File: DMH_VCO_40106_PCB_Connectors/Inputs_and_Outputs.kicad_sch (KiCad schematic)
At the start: 18 parts, among them J1 TS_Jack_6.35mm_Sw, J150 Conn_01x12, J2 TS_Jack_6.35mm_Sw, J200 IDC_02x05, J3 TS_Jack_6.35mm_Sw, J4 TS_Jack_6.35mm_Sw, J5 TS_Jack_6.35mm_Sw, J6 TS_Jack_6.35mm_Sw, J7 TS_Jack_6.35mm_Sw, J8 TS_Jack_6.35mm_Sw, J9 TS_Jack_6.35mm_Sw, SW1 SW_SPDT_321_OnOff, SW2 SW_SPDT_321_OnOff

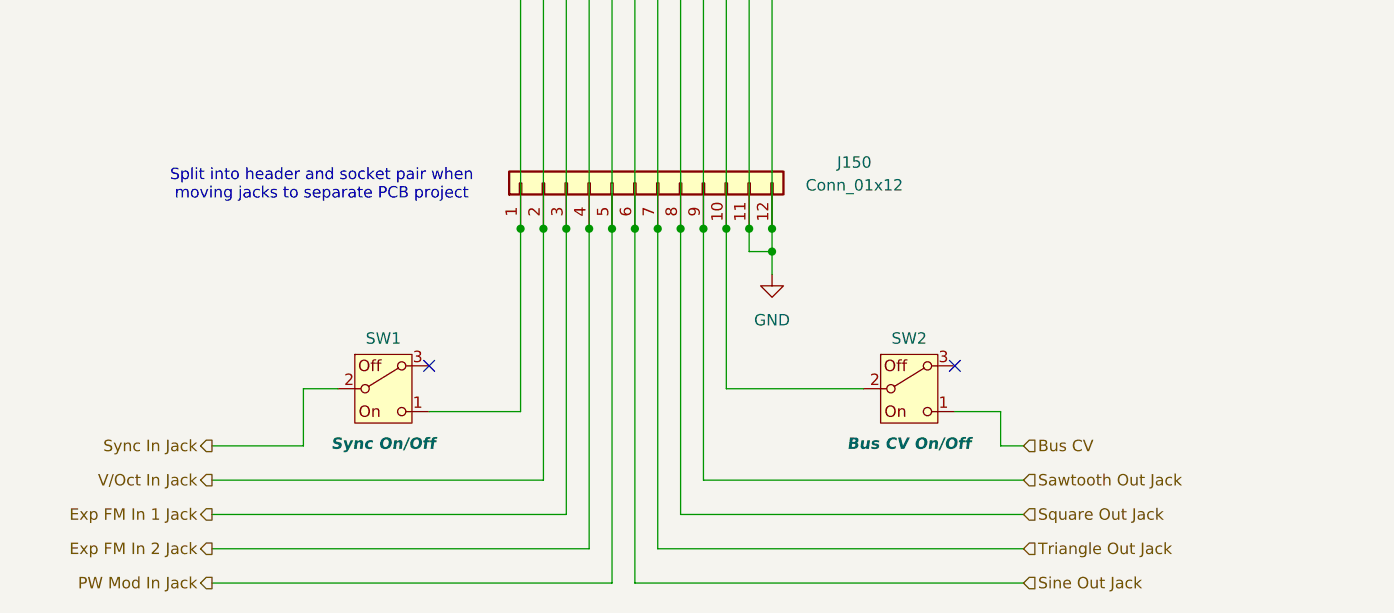
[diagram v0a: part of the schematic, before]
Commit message: Created separate connectors PCB
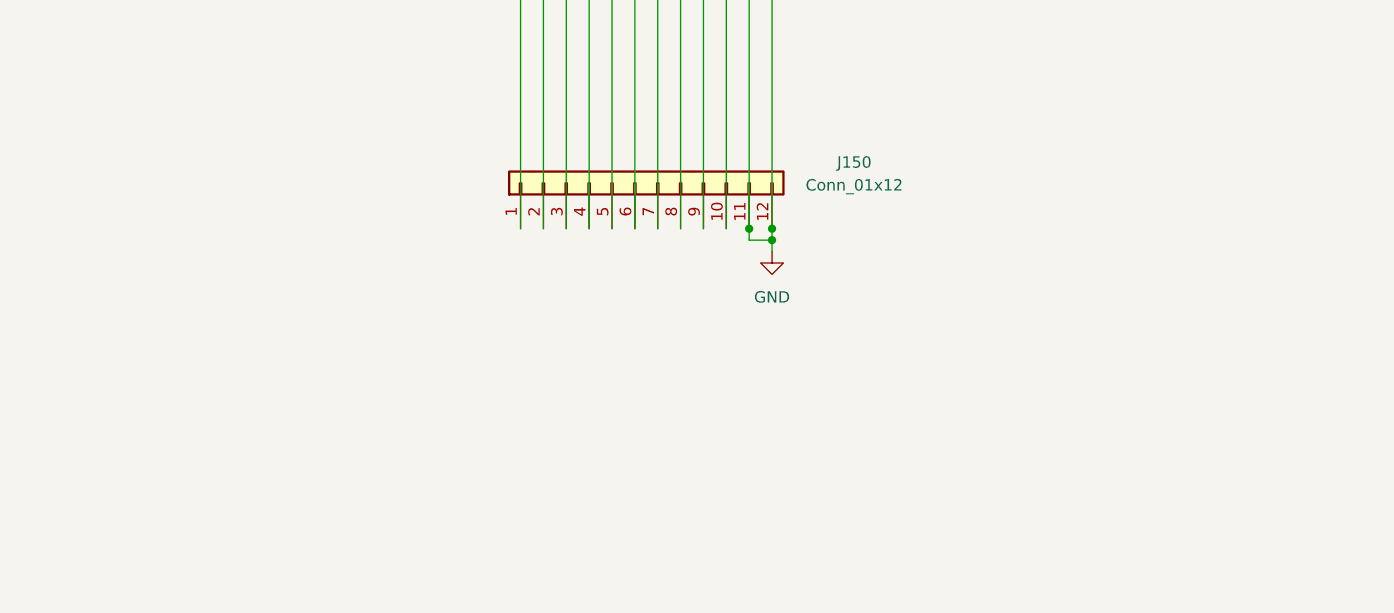
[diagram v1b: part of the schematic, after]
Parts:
- removed SW1, SW2: SW_SPDT_321_OnOff, SynthStuff:Toggle_Switch_THT, symbol SynthStuff:SW_SPDT_321_OnOff
- J150: footprint Connector_PinSocket_2.54mm:PinSocket_1x12_P2.54mm_Vertical -> Connector_PinHeader_2.54mm:PinHeader_1x12_P2.54mm_Vertical
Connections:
- net Exp FM In 1 Jack: no longer names the net of J150.3 (Pin_3), J3.T
- net Exp FM In 2 Jack: no longer names the net of J150.4 (Pin_4), J4.T
- net PW Mod In Jack: no longer names the net of J150.5 (Pin_5), J5.T
- net Sawtooth Out Jack: no longer names the net of J150.9 (Pin_9), R20.2
- net Sine Out Jack: no longer names the net of J150.6 (Pin_6), R44.1
- net Square Out Jack: no longer names the net of J150.8 (Pin_8), R21.2
- net Triangle Out Jack: no longer names the net of J150.7 (Pin_7), R28.1
- net V/Oct In Jack: no longer names the net of J150.2 (Pin_2), R7.1
- no-connect marks 4 -> 2
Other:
- note removed: "Split into header and socket pair when moving jacks to separate PCB project"

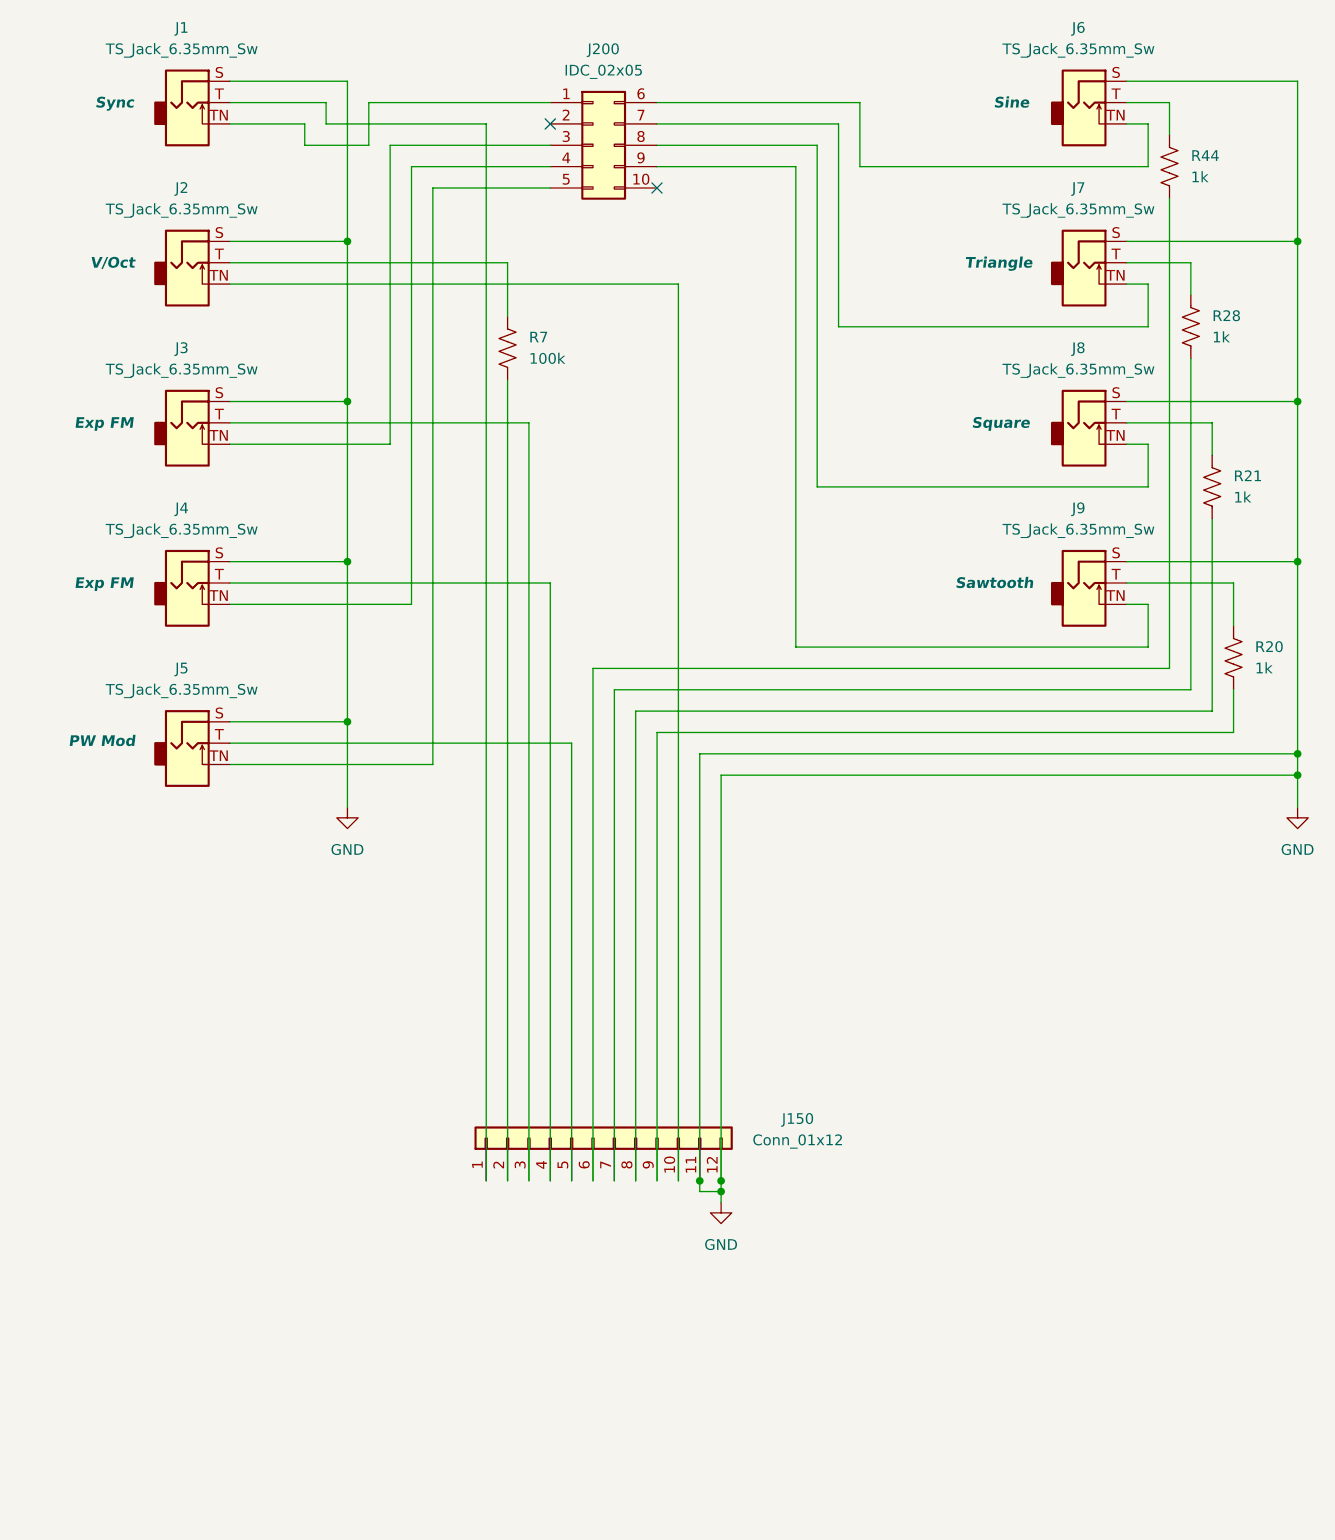
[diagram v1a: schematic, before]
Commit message: Placed input and output resistors back in main PCB
This ensures a more clear schematic and leaves the Connectors PCB only with actual connectors.
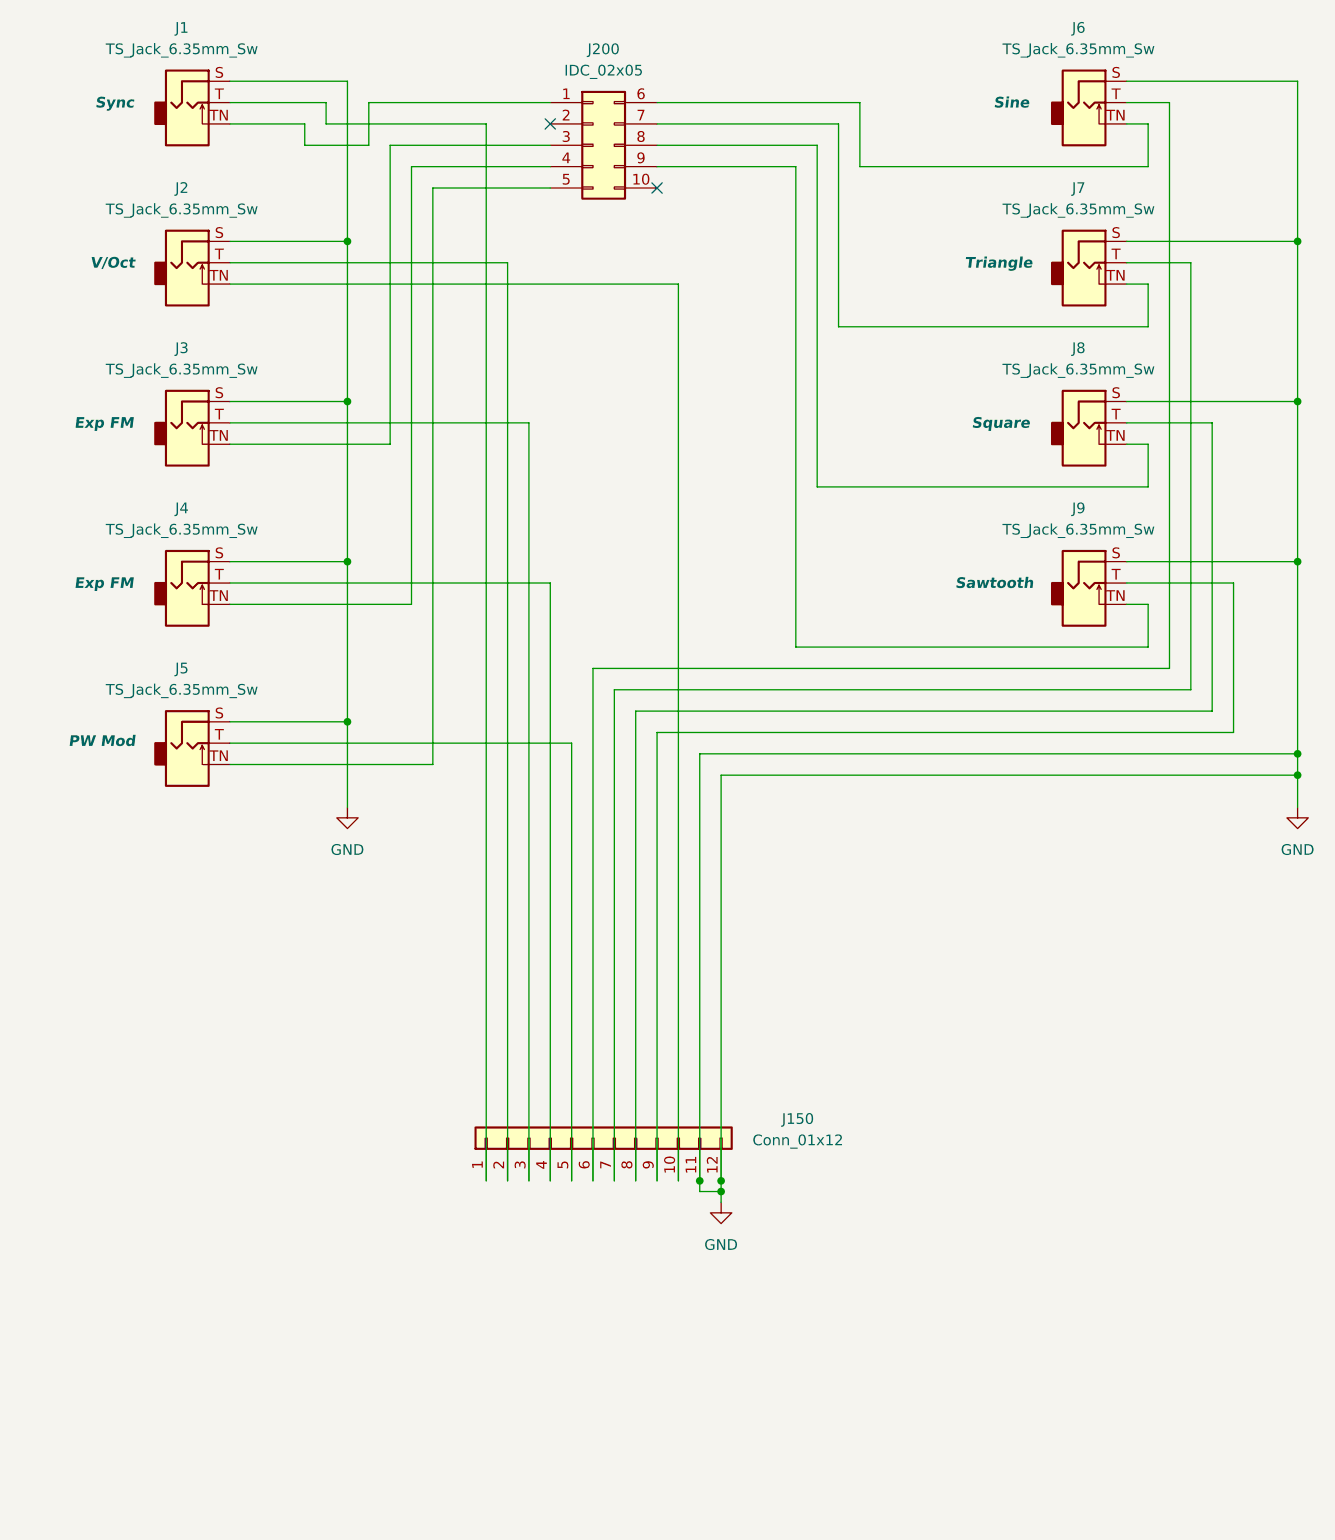
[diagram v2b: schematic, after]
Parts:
- removed R20, R21, R28, R44: 1k, Resistor_THT:R_Axial_DIN0207_L6.3mm_D2.5mm_P7.62mm_Horizontal, symbol Device:R_US
- removed R7: 100k, Resistor_THT:R_Axial_DIN0207_L6.3mm_D2.5mm_P7.62mm_Horizontal, symbol Device:R_US
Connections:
- net at J9.T: now also J150.9 (Pin_9)
- net at J2.T: now also J150.2 (Pin_2)
- net at J150.6 (Pin_6): now also J6.T
- net at J150.7 (Pin_7): now also J7.T
- net at J150.8 (Pin_8): now also J8.T

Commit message: Prepared PCBs for fabrication
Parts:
- J3: Function Exp FM -> Exp FM 1
- J4: Function Exp FM -> Exp FM 2
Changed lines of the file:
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@@
 			)
 		)
-		(property "Function" "Exp FM"
+		(property "Function" "Exp FM 1"
 			(at 54.864 63.5 0)
 			(effects
@@
 			)
 		)
-		(property "Function" "Exp FM"
+		(property "Function" "Exp FM 2"
 			(at 54.864 82.55 0)
 			(effects
